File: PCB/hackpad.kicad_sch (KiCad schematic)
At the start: 34 parts, among them SW1 SW_Push, SW10 SW_Push, SW11 SW_Push, SW12 SW_Push, SW13 SW_Push, SW14 SW_Push, SW15 SW_Push, SW16 SW_Push, SW2 SW_Push, SW3 SW_Push, SW4 SW_Push, SW5 SW_Push, SW6 SW_Push, SW7 SW_Push, SW8 SW_Push, SW9 SW_Push, U1 XIAO-RP2040-DIP

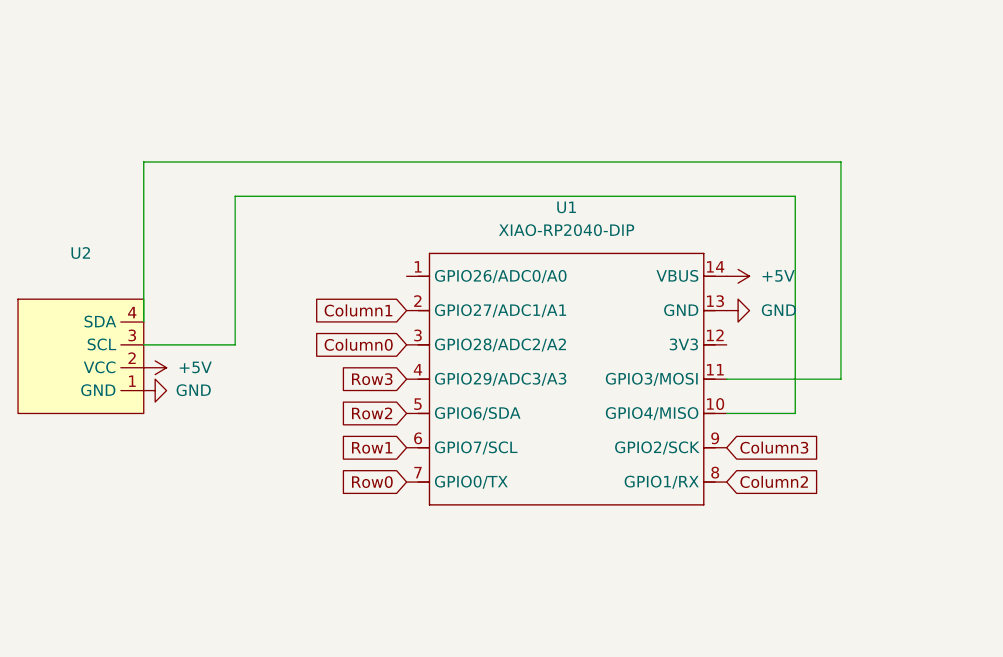
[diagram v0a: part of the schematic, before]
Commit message: Fix PCB for if anyone tries to use this project for refrence
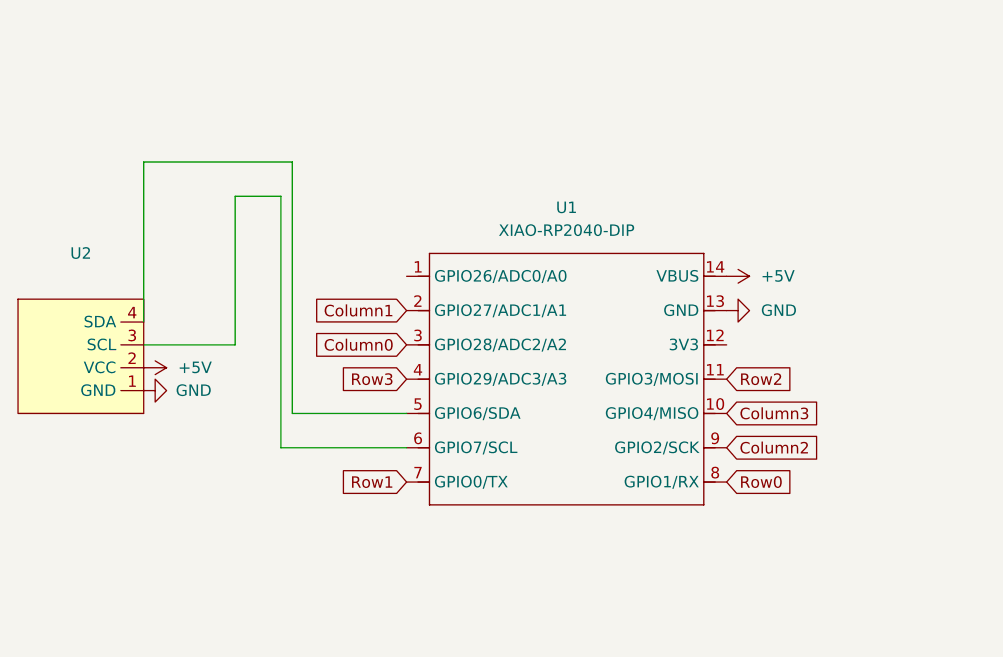
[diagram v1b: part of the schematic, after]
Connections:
- net Column2: now also U1.9 (GPIO2/SCK); no longer U1.8 (GPIO1/RX)
- net Column3: now also U1.10 (GPIO4/MISO); no longer U1.9 (GPIO2/SCK)
- net Row0: now also U1.8 (GPIO1/RX); no longer U1.7 (GPIO0/TX)
- net Row1: now also U1.7 (GPIO0/TX); no longer U1.6 (GPIO7/SCL)
- net Row2: now also U1.11 (GPIO3/MOSI); no longer U1.5 (GPIO6/SDA)
- net at U2.3 (SCL): now also U1.6 (GPIO7/SCL); no longer U1.10 (GPIO4/MISO)
- net at U2.4 (SDA): now also U1.5 (GPIO6/SDA); no longer U1.11 (GPIO3/MOSI)
